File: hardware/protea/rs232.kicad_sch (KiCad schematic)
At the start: 10 parts

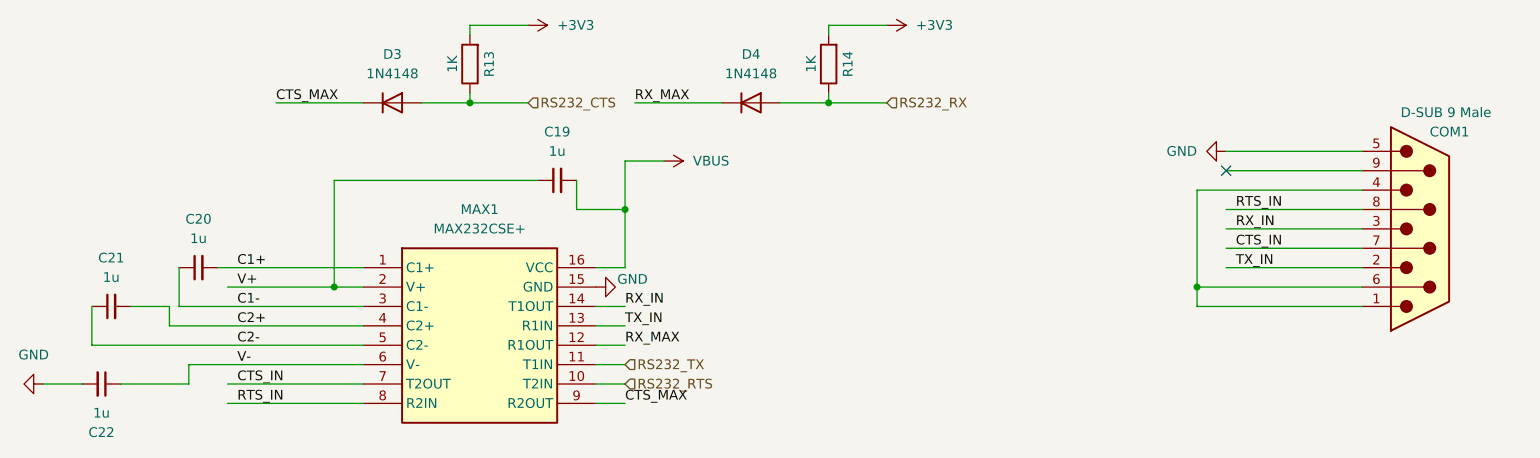
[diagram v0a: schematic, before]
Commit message: Versa renamed to Protea
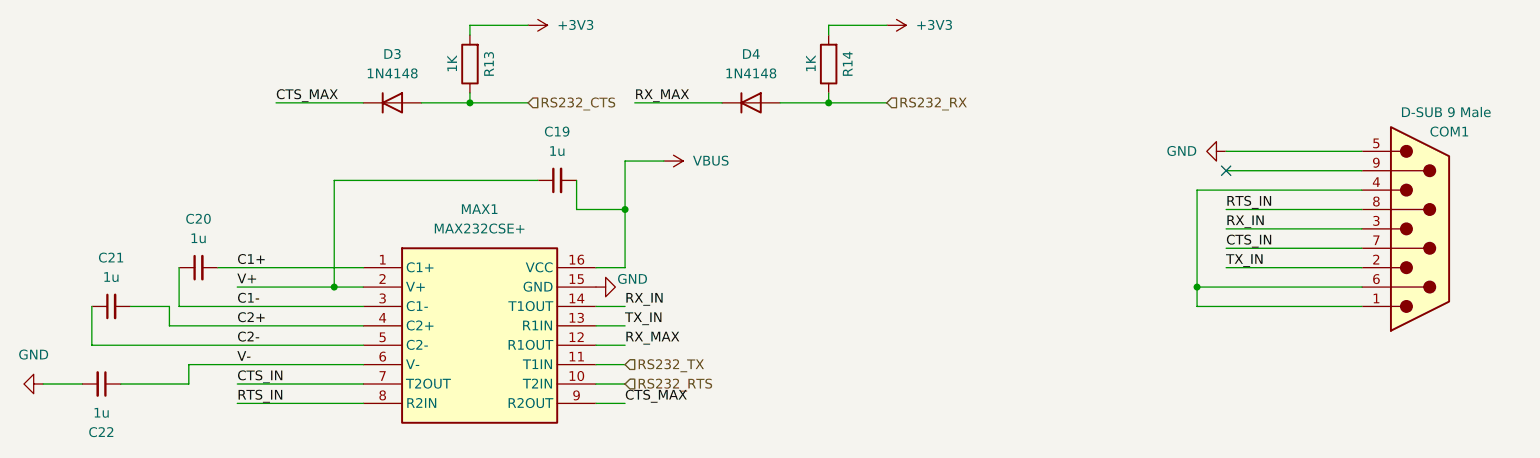
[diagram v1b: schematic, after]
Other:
- title: VersaTerm -> Protea
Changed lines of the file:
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@@
 (kicad_sch
-	(version 20231120)
+	(version 20250114)
 	(generator "eeschema")
-	(generator_version "8.0")
+	(generator_version "9.0")
 	(paper "A4")
 	(title_block
-		(title "VersaTerm")
-		(date "2025-02-03")
-		(rev "2.01")
+		(title "Protea")
+		(date "2025-03-03")
+		(rev "2.02")
 		(company "Mikhail Matveev")
 		(comment 1 "https://github.com/xtremespb/frank")
@@
 	(wire
 		(pts
-			(xy 63.5 86.36) (xy 81.28 86.36)
+			(xy 64.77 86.36) (xy 81.28 86.36)
 		)
 		(stroke
@@
 	(wire
 		(pts
+			(xy 55.88 73.66) (xy 55.88 76.2)
+		)
+		(stroke
+			(width 0)
+			(type default)
+		)
+	)
+	(wire
+		(pts
+			(xy 111.76 86.36) (xy 115.57 86.36)
+		)
+		(stroke
+			(width 0)
+			(type default)
+		)
+	)
+	(wire
+		(pts
+			(xy 55.88 76.2) (xy 81.28 76.2)
+		)
+		(stroke
+			(width 0)
+			(type default)
+		)
+	)
+	(wire
+		(pts
+			(xy 102.87 36.83) (xy 95.25 36.83)
+		)
+		(stroke
+			(width 0)
+			(type default)
+		)
+	)
+	(wire
+		(pts
+			(xy 194.31 53.34) (xy 212.09 53.34)
+		)
+		(stroke
+			(width 0)
+			(type default)
+		)
+	)
+	(wire
+		(pts
+			(xy 149.86 36.83) (xy 142.24 36.83)
+		)
+		(stroke
+			(width 0)
+			(type default)
+		)
+	)
+	(wire
+		(pts
+			(xy 45.72 73.66) (xy 45.72 78.74)
+		)
+		(stroke
+			(width 0)
+			(type default)
+		)
+	)
+	(wire
+		(pts
+			(xy 194.31 63.5) (xy 212.09 63.5)
+		)
+		(stroke
+			(width 0)
+			(type default)
+		)
+	)
+	(wire
+		(pts
+			(xy 64.77 83.82) (xy 81.28 83.82)
+		)
+		(stroke
+			(width 0)
+			(type default)
+		)
+	)
+	(wire
+		(pts
 			(xy 194.31 60.96) (xy 212.09 60.96)
 		)
@@
 	(wire
 		(pts
-			(xy 55.88 73.66) (xy 55.88 76.2)
-		)
-		(stroke
-			(width 0)
-			(type default)
-		)
-	)
-	(wire
-		(pts
-			(xy 111.76 86.36) (xy 115.57 86.36)
-		)
-		(stroke
-			(width 0)
-			(type default)
-		)
-	)
-	(wire
-		(pts
-			(xy 55.88 76.2) (xy 81.28 76.2)
-		)
-		(stroke
-			(width 0)
-			(type default)
-		)
-	)
-	(wire
-		(pts
-			(xy 102.87 36.83) (xy 95.25 36.83)
-		)
-		(stroke
-			(width 0)
-			(type default)
-		)
-	)
-	(wire
-		(pts
-			(xy 194.31 53.34) (xy 212.09 53.34)
-		)
-		(stroke
-			(width 0)
-			(type default)
-		)
-	)
-	(wire
-		(pts
-			(xy 149.86 36.83) (xy 142.24 36.83)
-		)
-		(stroke
-			(width 0)
-			(type default)
-		)
-	)
-	(wire
-		(pts
-			(xy 45.72 73.66) (xy 45.72 78.74)
-		)
-		(stroke
-			(width 0)
-			(type default)
-		)
-	)
-	(wire
-		(pts
-			(xy 63.5 83.82) (xy 81.28 83.82)
-		)
-		(stroke
-			(width 0)
-			(type default)
-		)
-	)
-	(wire
-		(pts
-			(xy 63.5 71.12) (xy 77.47 71.12)
+			(xy 64.77 71.12) (xy 77.47 71.12)
 		)
 		(stroke
@@
 		(pts
 			(xy 69.85 46.99) (xy 81.28 46.99)
-		)
-		(stroke
-			(width 0)
-			(type default)
-		)
-	)
-	(wire
-		(pts
-			(xy 194.31 63.5) (xy 212.09 63.5)
 		)
 		(stroke
@@
 	(label "CTS_MAX"
 		(at 115.57 86.36 0)
-		(fields_autoplaced yes)
 		(effects
 			(font
@@
 	(label "RX_IN"
 		(at 115.57 73.66 0)
-		(fields_autoplaced yes)
 		(effects
 			(font
@@
 	(label "CTS_IN"
 		(at 64.77 83.82 0)
-		(fields_autoplaced yes)
 		(effects
 			(font
@@
 	(label "CTS_MAX"
 		(at 69.85 46.99 0)
-		(fields_autoplaced yes)
 		(effects
 			(font
@@
 	(label "RX_MAX"
 		(at 116.84 46.99 0)
-		(fields_autoplaced yes)
 		(effects
 			(font
@@
 	)
 	(label "TX_IN"
-		(at 195.58 68.58 0)
-		(fields_autoplaced yes)
+		(at 194.31 68.58 0)
 		(effects
 			(font
@@
 	(label "C1-"
 		(at 64.77 73.66 0)
-		(fields_autoplaced yes)
 		(effects
 			(font
@@
 	(label "V-"
 		(at 64.77 81.28 0)
-		(fields_autoplaced yes)
 		(effects
 			(font
@@
 	)
 	(label "RTS_IN"
-		(at 195.58 60.96 0)
-		(fields_autoplaced yes)
+		(at 194.31 60.96 0)
 		(effects
 			(font
@@
 	(label "C2-"
 		(at 64.77 78.74 0)
-		(fields_autoplaced yes)
 		(effects
 			(font
@@
 	(label "RX_MAX"
 		(at 115.57 78.74 0)
-		(fields_autoplaced yes)
 		(effects
 			(font
@@
 	(label "C1+"
 		(at 64.77 68.58 0)
-		(fields_autoplaced yes)
 		(effects
 			(font
@@
 	(label "RTS_IN"
 		(at 64.77 86.36 0)
-		(fields_autoplaced yes)
 		(effects
 			(font
@@
 	(label "C2+"
 		(at 64.77 76.2 0)
-		(fields_autoplaced yes)
 		(effects
 			(font
@@
 	)
 	(label "CTS_IN"
-		(at 195.58 66.04 0)
-		(fields_autoplaced yes)
+		(at 194.31 66.04 0)
 		(effects
 			(font
@@
 	(label "TX_IN"
 		(at 115.57 76.2 0)
-		(fields_autoplaced yes)
 		(effects
 			(font
@@
 	)
 	(label "RX_IN"
-		(at 195.58 63.5 0)
-		(fields_autoplaced yes)
+		(at 194.31 63.5 0)
 		(effects
 			(font
@@
 	(label "V+"
 		(at 64.77 71.12 0)
-		(fields_autoplaced yes)
 		(effects
 			(font
@@
 		(shape input)
 		(at 149.86 46.99 0)
-		(fields_autoplaced yes)
 		(effects
 			(font
@@
 		(shape input)
 		(at 102.87 46.99 0)
-		(fields_autoplaced yes)
 		(effects
 			(font
@@
 		(shape input)
 		(at 115.57 83.82 0)
-		(fields_autoplaced yes)
 		(effects
 			(font
@@
 		(shape input)
 		(at 115.57 81.28 0)
-		(fields_autoplaced yes)
-		(effects
-			(font
+		(effects
+			(font
